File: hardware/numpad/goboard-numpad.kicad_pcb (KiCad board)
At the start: 2 copper layers, 74.9 x 104.1 mm, 46 parts, among them J1 Conn_02x05_Top_Bottom, J2 Conn_01x01, J3 Conn_01x05, J4 Conn_01x02_Female, J5 Conn_01x02_Male, SW1 SW_Push, SW10 5, SW12 2, SW13 dot, SW14 times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

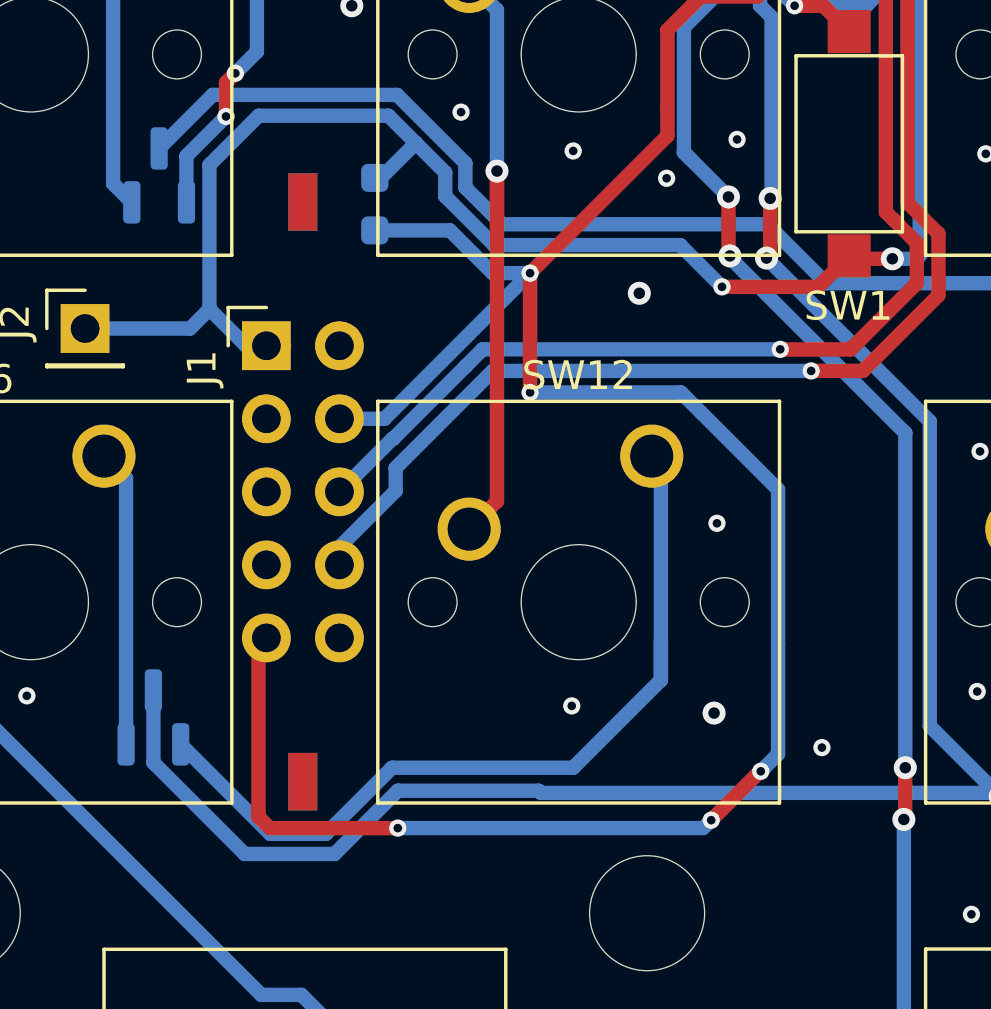
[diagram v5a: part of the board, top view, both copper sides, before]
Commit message: Main & Numpad: Fix the pin-out of the programmer connector
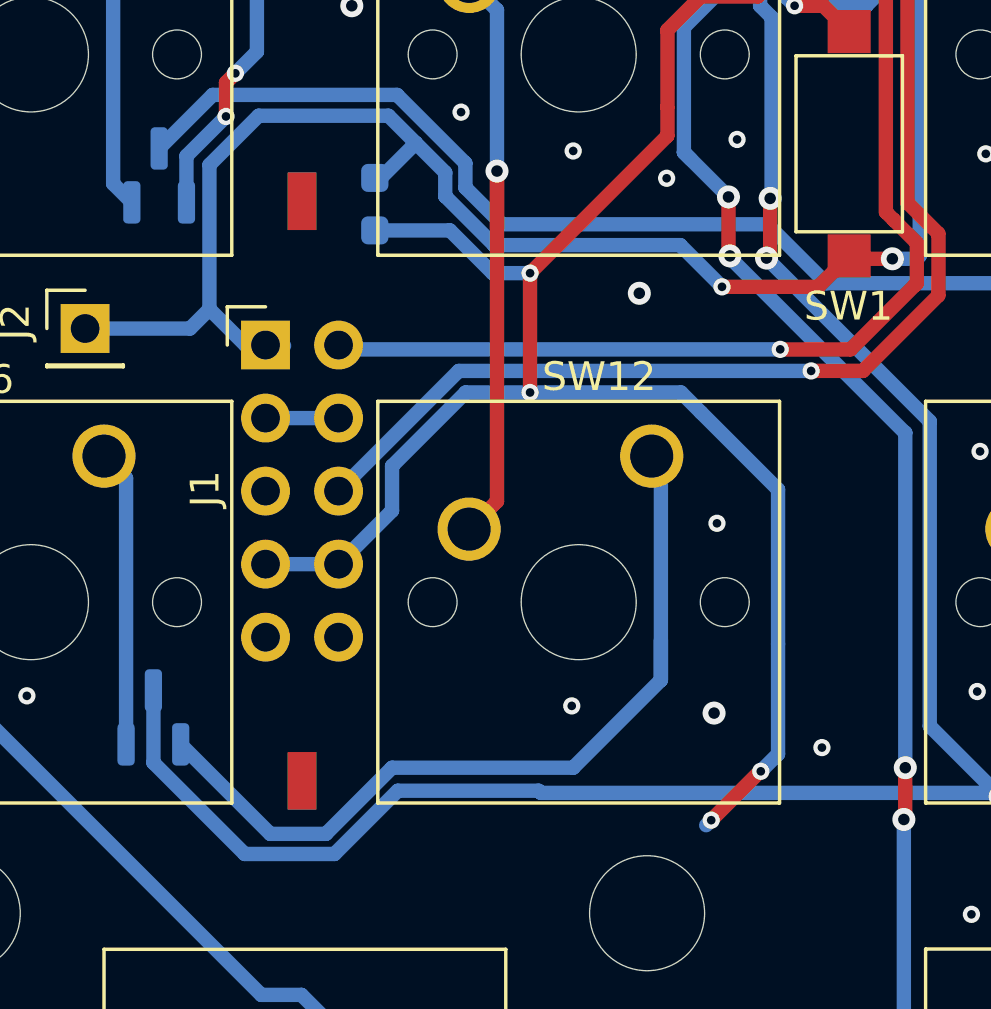
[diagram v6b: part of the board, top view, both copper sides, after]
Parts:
- J1: value Conn_02x05_Top_Bottom -> Conn_02x05_Odd_Even
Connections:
- J1 pad 2: GND -> /SWDIO
- J1 pad 3: unconnected-(J1-Pad3) -> GND
- J1 pad 4: VCC -> GND
- J1 pad 6: /SWDIO -> /SWDCLK
- J1 pad 7: GND -> VCC
- J1 pad 8: /SWDCLK -> VCC
- J1 pad 9: VCC -> unconnected-(J1-Pad9)
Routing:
- net VCC: track 224.7 -> 207.2 mm, vias 11 -> 10
- net GND: track 18.9 -> 21.5 mm
- net /SWDIO: track 48.8 -> 46.8 mm
- net /SWDCLK: track 50.2 -> 48.4 mm

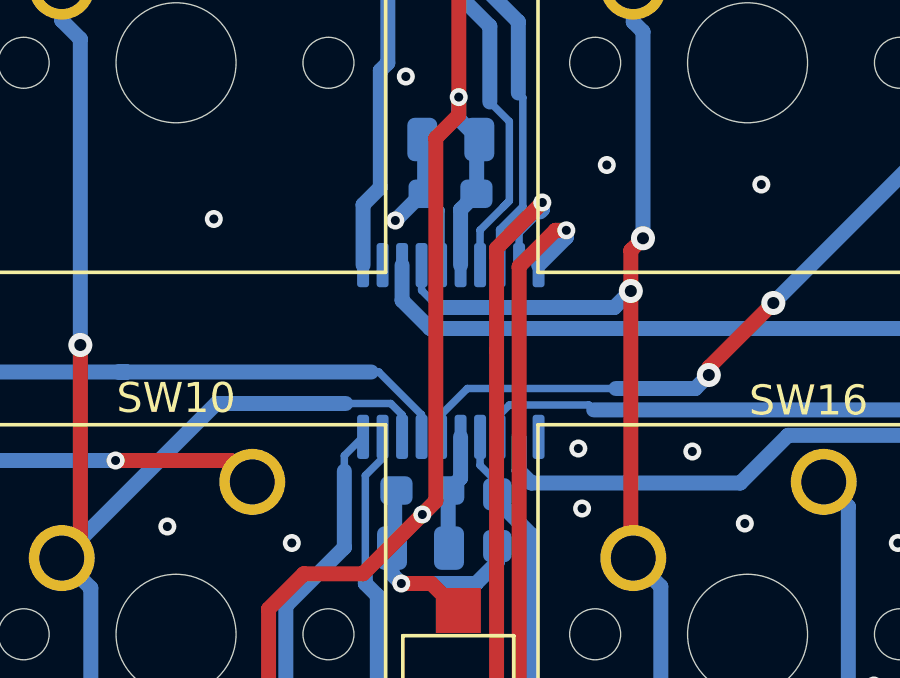
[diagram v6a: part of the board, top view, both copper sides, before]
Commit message: Numpad: Exchange MCU for an available version
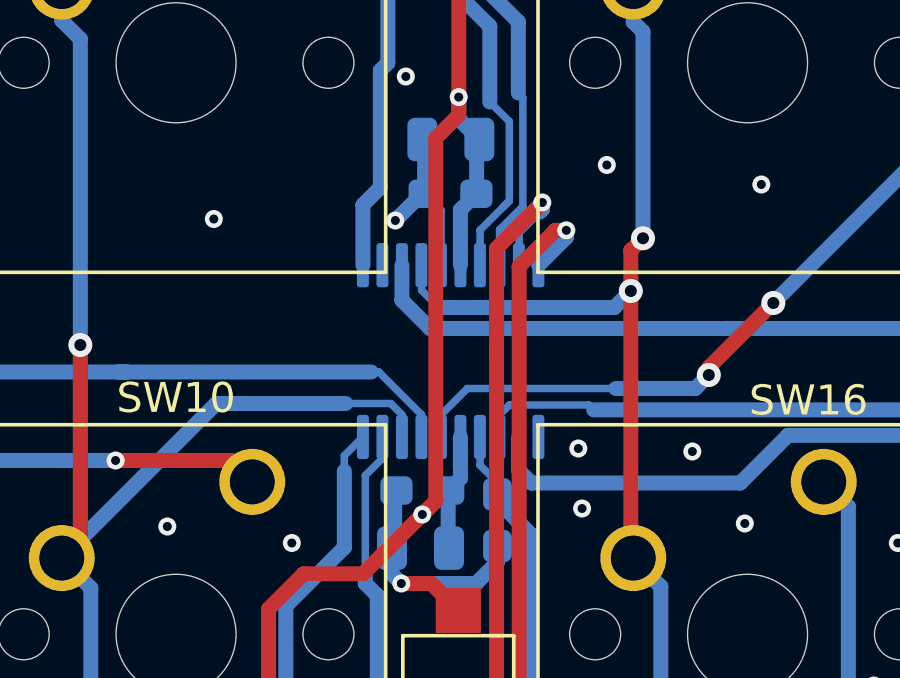
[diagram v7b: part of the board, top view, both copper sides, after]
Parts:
- U1: value STM32L011F4Px -> STM32L031F6Px

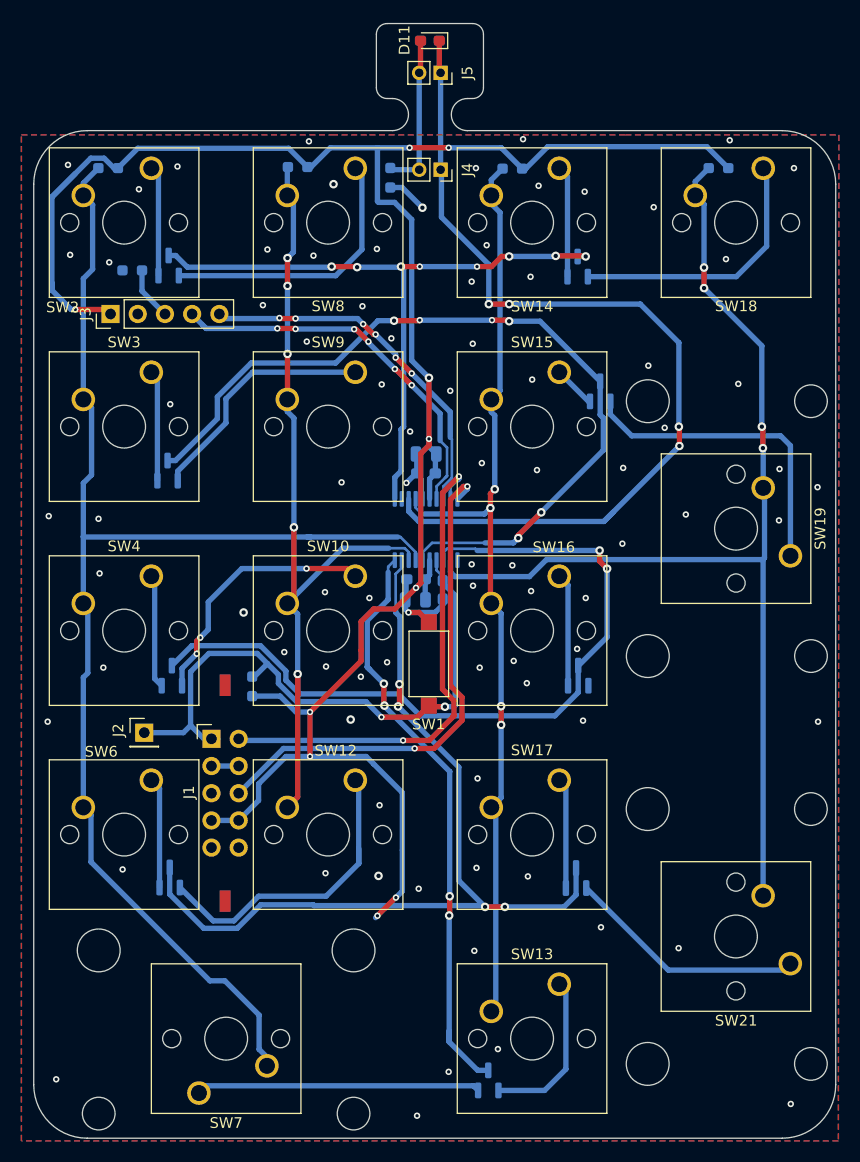
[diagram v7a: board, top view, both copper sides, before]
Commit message: Numpad: Add mounting holes
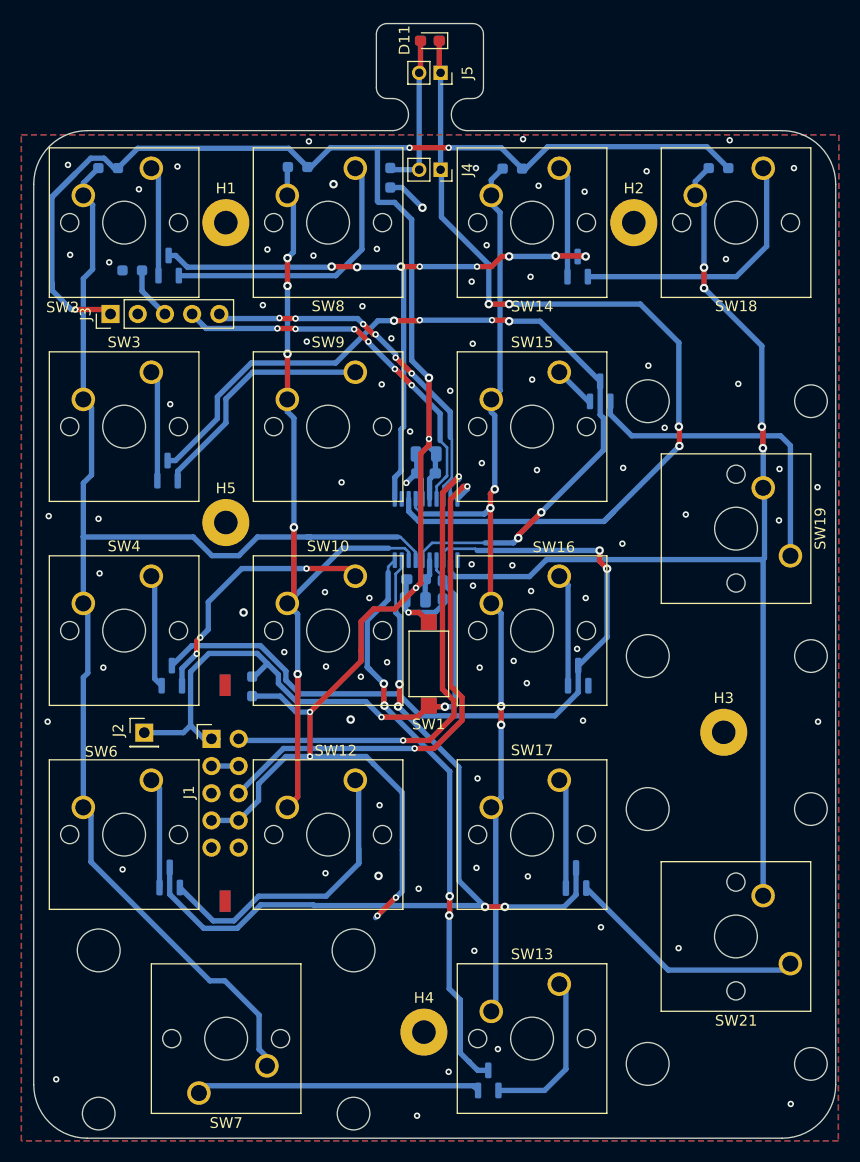
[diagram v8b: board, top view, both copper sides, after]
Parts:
- added H1: MountingHole, MountingHole:MountingHole_2.2mm_M2_Pad, F.Cu at (123.6, 67.0)
- added H2: MountingHole, MountingHole:MountingHole_2.2mm_M2_Pad, F.Cu at (161.7, 67.0)
- added H3: MountingHole, MountingHole:MountingHole_2.2mm_M2_Pad, F.Cu at (170.1, 114.6)
- added H4: MountingHole, MountingHole:MountingHole_2.2mm_M2_Pad, F.Cu at (142.1, 142.6)
- added H5: MountingHole, MountingHole:MountingHole_2.2mm_M2_Pad, F.Cu at (123.6, 95.0)
- C1: value 0,1u -> 100n
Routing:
- net /Keys/COLUMN_0: track 126.7 -> 128.2 mm
- net /Keys/ROW_4: track 55.4 -> 54.4 mm
